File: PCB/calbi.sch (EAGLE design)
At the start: 32 parts, among them U1 LT3086MPT7, U2 33MHZ-OSCILLATOR

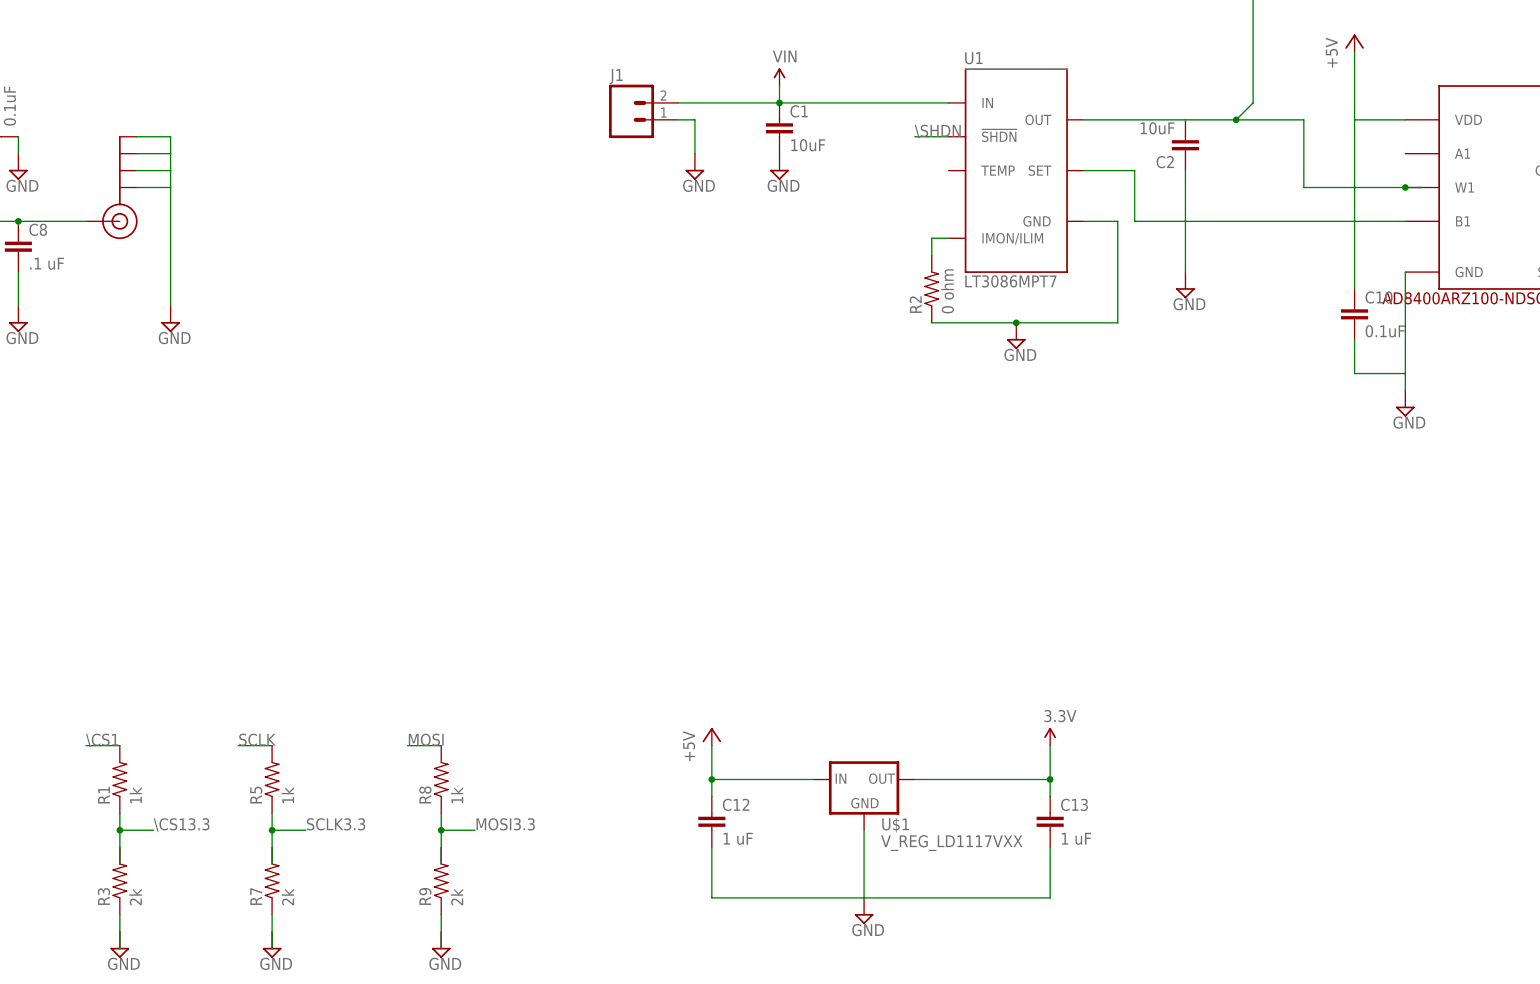
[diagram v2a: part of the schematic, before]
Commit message: Fixed a couple of errors in the schematic. Layed out power. Going to meet on Wednesday at 3:30 to do the RF layout
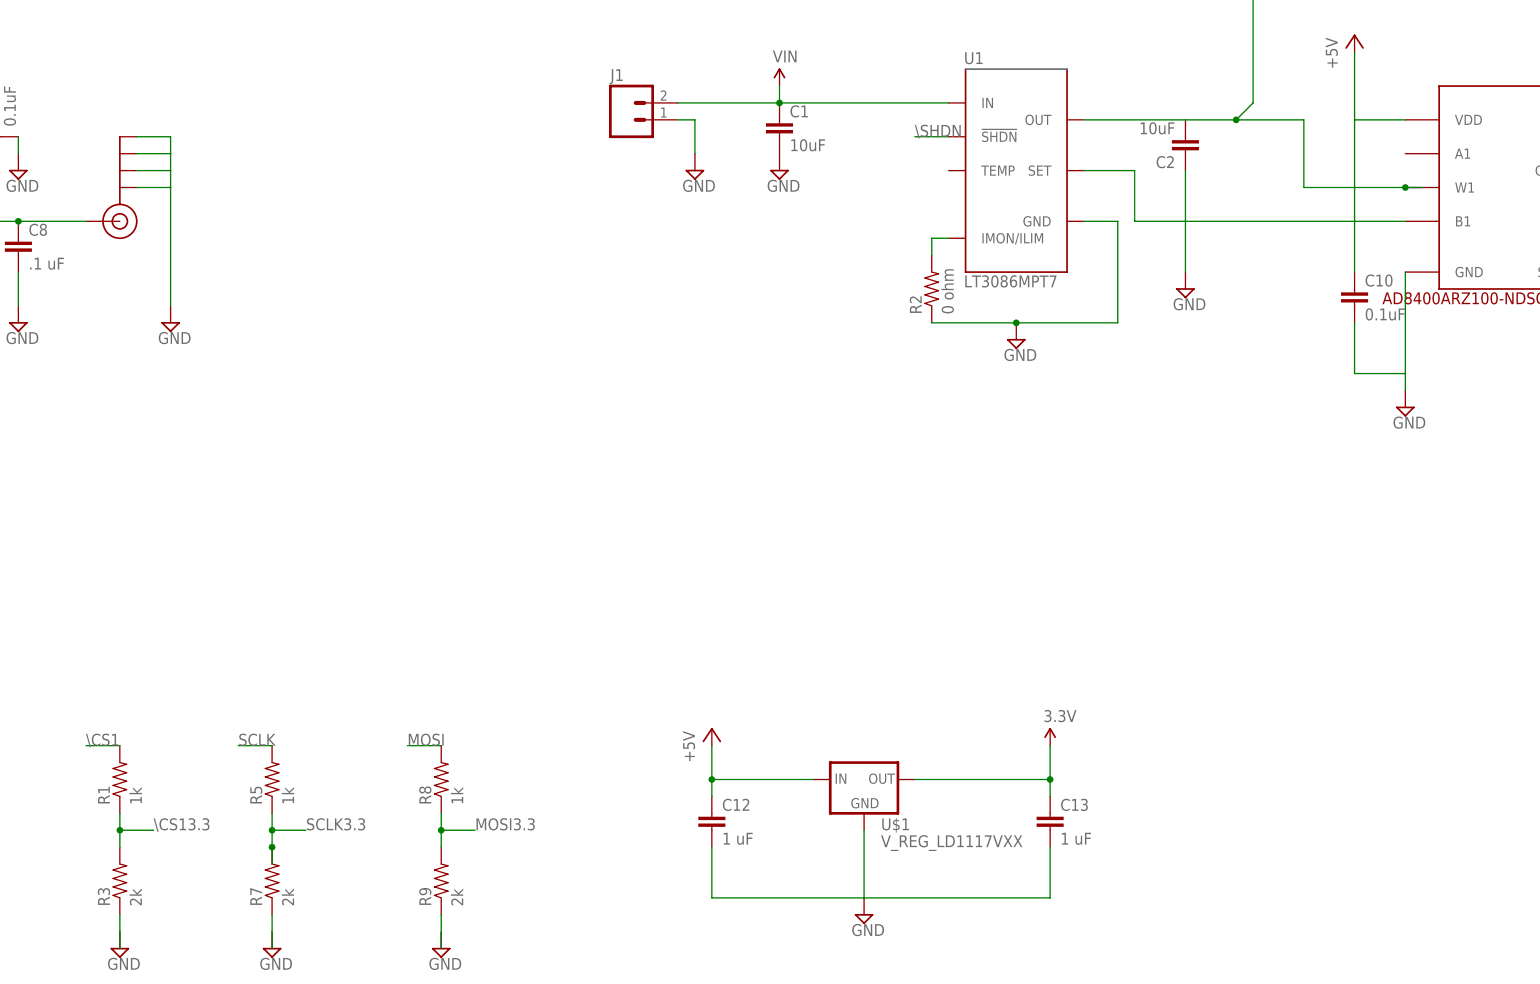
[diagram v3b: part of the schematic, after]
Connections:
- net MOSI3.3: now also R9.2
- net SCLK3.3: now also R7.2
- net \CS13.3: now also R3.2
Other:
- moved on the sheet: C10
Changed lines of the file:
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@@
 <instance part="U$3" gate="G$1" x="149.86" y="198.12" rot="MR0"/>
 <instance part="C2" gate="G$1" x="101.6" y="210.82" rot="R180"/>
-<instance part="C10" gate="G$1" x="127" y="182.88"/>
+<instance part="C10" gate="G$1" x="127" y="185.42"/>
 <instance part="SUPPLY14" gate="GND" x="134.62" y="170.18"/>
 <instance part="SUPPLY16" gate="GND" x="101.6" y="187.96"/>
@@
 <pinref part="C10" gate="G$1" pin="2"/>
 <wire x1="134.62" y1="175.26" x2="134.62" y2="172.72" width="0.1524" layer="91"/>
-<wire x1="127" y1="180.34" x2="127" y2="175.26" width="0.1524" layer="91"/>
+<wire x1="127" y1="182.88" x2="127" y2="175.26" width="0.1524" layer="91"/>
 <wire x1="127" y1="175.26" x2="134.62" y2="175.26" width="0.1524" layer="91"/>
 </segment>
@@
 <pinref part="U$3" gate="G$1" pin="VDD"/>
 <wire x1="134.62" y1="213.36" x2="127" y2="213.36" width="0.1524" layer="91"/>
-<wire x1="127" y1="213.36" x2="127" y2="187.96" width="0.1524" layer="91"/>
+<wire x1="127" y1="213.36" x2="127" y2="190.5" width="0.1524" layer="91"/>
 <pinref part="C10" gate="G$1" pin="1"/>
 <pinref part="P+1" gate="1" pin="+5V"/>
@@
 <pinref part="R5" gate="G$1" pin="1"/>
 <wire x1="-35.56" y1="109.22" x2="-35.56" y2="106.68" width="0.1524" layer="91"/>
-<wire x1="-35.56" y1="106.68" x2="-35.56" y2="101.6" width="0.1524" layer="91"/>
 <wire x1="-35.56" y1="106.68" x2="-30.48" y2="106.68" width="0.1524" layer="91"/>
+<label x="-30.48" y="106.68" size="1.778" layer="95"/>
+<pinref part="R7" gate="G$1" pin="2"/>
+<wire x1="-35.56" y1="104.14" x2="-35.56" y2="101.6" width="0.1524" layer="91"/>
+<wire x1="-35.56" y1="106.68" x2="-35.56" y2="104.14" width="0.1524" layer="91"/>
 <junction x="-35.56" y="106.68"/>
-<label x="-30.48" y="106.68" size="1.778" layer="95"/>
+<junction x="-35.56" y="104.14"/>
 </segment>
 </net>
@@
 <pinref part="R8" gate="G$1" pin="1"/>
 <wire x1="-10.16" y1="109.22" x2="-10.16" y2="106.68" width="0.1524" layer="91"/>
-<wire x1="-10.16" y1="106.68" x2="-10.16" y2="101.6" width="0.1524" layer="91"/>
 <wire x1="-10.16" y1="106.68" x2="-5.08" y2="106.68" width="0.1524" layer="91"/>
+<label x="-5.08" y="106.68" size="1.778" layer="95"/>
+<pinref part="R9" gate="G$1" pin="2"/>
+<wire x1="-10.16" y1="106.68" x2="-10.16" y2="104.14" width="0.1524" layer="91"/>
 <junction x="-10.16" y="106.68"/>
-<label x="-5.08" y="106.68" size="1.778" layer="95"/>
 </segment>
 </net>
@@
 <pinref part="R1" gate="G$1" pin="1"/>
 <wire x1="-58.42" y1="109.22" x2="-58.42" y2="106.68" width="0.1524" layer="91"/>
-<wire x1="-58.42" y1="106.68" x2="-58.42" y2="101.6" width="0.1524" layer="91"/>
 <wire x1="-58.42" y1="106.68" x2="-53.34" y2="106.68" width="0.1524" layer="91"/>
+<label x="-53.34" y="106.68" size="1.778" layer="95"/>
+<pinref part="R3" gate="G$1" pin="2"/>
+<wire x1="-58.42" y1="106.68" x2="-58.42" y2="104.14" width="0.1524" layer="91"/>
 <junction x="-58.42" y="106.68"/>
-<label x="-53.34" y="106.68" size="1.778" layer="95"/>
-</segment>
-</net>
+</segment>
+</net>

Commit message: Commiting changes from Wednesday
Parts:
- C11: value .1 uF -> 0.1uF
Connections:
- net 3.3V: now also C11.1; no longer U2.GND
- net GND: now also C11.2, U2.GND
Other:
- moved on the sheet: C11
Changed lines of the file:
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@@
 <part name="SUPPLY16" library="supply2" deviceset="GND" device=""/>
 <part name="U2" library="SparkFun-FreqCtrl" deviceset="33MHZ-OSCILLATOR" device=""/>
-<part name="C11" library="SparkFun-Capacitors" deviceset="CAP" device="0603-CAP" value=".1 uF"/>
 <part name="SUPPLY17" library="supply2" deviceset="GND" device=""/>
 <part name="SUPPLY18" library="SparkFun-Aesthetics" deviceset="3.3V" device=""/>
@@
 <part name="P+3" library="supply1" deviceset="+5V" device=""/>
 <part name="SUPPLY27" library="SparkFun-Aesthetics" deviceset="3.3V" device=""/>
+<part name="C11" library="SparkFun-Capacitors" deviceset="CAP" device="0603-CAP" value="0.1uF"/>
+<part name="SUPPLY28" library="supply2" deviceset="GND" device=""/>
 </parts>
 <sheets>
@@
 <instance part="SUPPLY16" gate="GND" x="101.6" y="187.96"/>
 <instance part="U2" gate="G$1" x="-152.4" y="165.1"/>
-<instance part="C11" gate="G$1" x="-177.8" y="163.068"/>
-<instance part="SUPPLY17" gate="GND" x="-177.8" y="154.94"/>
+<instance part="SUPPLY17" gate="GND" x="-177.8" y="144.78"/>
 <instance part="SUPPLY18" gate="G$1" x="-177.8" y="172.72"/>
 <instance part="P+1" gate="1" x="127" y="226.06"/>
@@
 <instance part="P+3" gate="1" x="30.48" y="121.92"/>
 <instance part="SUPPLY27" gate="G$1" x="81.28" y="119.38"/>
+<instance part="C11" gate="G$1" x="-177.8" y="157.48"/>
+<instance part="SUPPLY28" gate="GND" x="-139.7" y="154.94"/>
 </instances>
 <busses>
@@
 <wire x1="-177.8" y1="172.72" x2="-177.8" y2="167.64" width="0.1524" layer="91"/>
 <pinref part="U2" gate="G$1" pin="VCC"/>
-<wire x1="-177.8" y1="167.64" x2="-177.8" y2="157.48" width="0.1524" layer="91"/>
-<wire x1="-177.8" y1="157.48" x2="-177.8" y2="154.94" width="0.1524" layer="91"/>
 <wire x1="-165.1" y1="167.64" x2="-177.8" y2="167.64" width="0.1524" layer="91"/>
 <junction x="-177.8" y="167.64"/>
-<pinref part="U2" gate="G$1" pin="GND"/>
-<wire x1="-139.7" y1="162.56" x2="-139.7" y2="157.48" width="0.1524" layer="91"/>
-<wire x1="-139.7" y1="157.48" x2="-177.8" y2="157.48" width="0.1524" layer="91"/>
-<junction x="-177.8" y="157.48"/>
+<pinref part="C11" gate="G$1" pin="1"/>
+<wire x1="-177.8" y1="162.56" x2="-177.8" y2="167.64" width="0.1524" layer="91"/>
 </segment>
 <segment>
@@
 </segment>
 <segment>
-<pinref part="C9" gate="G$1" pin="2"/>
-<pinref part="SUPPLY15" gate="GND" pin="GND"/>
-<wire x1="-96.52" y1="114.3" x2="-96.52" y2="111.76" width="0.1524" layer="91"/>
-</segment>
-<segment>
 <pinref part="SUPPLY20" gate="GND" pin="GND"/>
 <pinref part="_1" gate="G$1" pin="_GND"/>
@@
 <wire x1="81.28" y1="96.52" x2="81.28" y2="104.14" width="0.1524" layer="91"/>
 </segment>
+<segment>
+<pinref part="SUPPLY17" gate="GND" pin="GND"/>
+<wire x1="-177.8" y1="154.94" x2="-177.8" y2="147.32" width="0.1524" layer="91"/>
+<pinref part="C11" gate="G$1" pin="2"/>
+</segment>
+<segment>
+<pinref part="U2" gate="G$1" pin="GND"/>
+<wire x1="-139.7" y1="162.56" x2="-139.7" y2="157.48" width="0.1524" layer="91"/>
+<pinref part="SUPPLY28" gate="GND" pin="GND"/>
+</segment>
+<segment>
+<pinref part="C9" gate="G$1" pin="2"/>
+<pinref part="SUPPLY15" gate="GND" pin="GND"/>
+<wire x1="-96.52" y1="114.3" x2="-96.52" y2="111.76" width="0.1524" layer="91"/>
+</segment>
 </net>

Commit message: FInished up a few things. Set up the cam.
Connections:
- removed net N$12: R7.1
- removed net N$13: R9.1
- removed net N$9: R3.1
- net GND: now also R3.1, R7.1, R9.1
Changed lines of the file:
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@@
 <instance part="R1" gate="G$1" x="-58.42" y="114.3" rot="R90"/>
 <instance part="R3" gate="G$1" x="-58.42" y="99.06" rot="R90"/>
-<instance part="SUPPLY21" gate="GND" x="-58.42" y="88.9"/>
+<instance part="SUPPLY21" gate="GND" x="-58.42" y="83.82"/>
 <instance part="R5" gate="G$1" x="-35.56" y="114.3" rot="R90"/>
 <instance part="R7" gate="G$1" x="-35.56" y="99.06" rot="R90"/>
-<instance part="SUPPLY22" gate="GND" x="-35.56" y="88.9"/>
+<instance part="SUPPLY22" gate="GND" x="-35.56" y="83.82"/>
 <instance part="R8" gate="G$1" x="-10.16" y="114.3" rot="R90"/>
 <instance part="R9" gate="G$1" x="-10.16" y="99.06" rot="R90"/>
-<instance part="SUPPLY23" gate="GND" x="-10.16" y="88.9"/>
+<instance part="SUPPLY23" gate="GND" x="-10.16" y="83.82"/>
 <instance part="SUPPLY24" gate="G$1" x="40.64" y="218.44"/>
 <instance part="J1" gate="G$1" x="17.78" y="213.36"/>
@@
 <wire x1="-96.52" y1="114.3" x2="-96.52" y2="111.76" width="0.1524" layer="91"/>
 </segment>
+<segment>
+<pinref part="R7" gate="G$1" pin="1"/>
+<wire x1="-35.56" y1="93.98" x2="-35.56" y2="86.36" width="0.1524" layer="91"/>
+<pinref part="SUPPLY22" gate="GND" pin="GND"/>
+</segment>
+<segment>
+<pinref part="R9" gate="G$1" pin="1"/>
+<wire x1="-10.16" y1="93.98" x2="-10.16" y2="86.36" width="0.1524" layer="91"/>
+<pinref part="SUPPLY23" gate="GND" pin="GND"/>
+</segment>
+<segment>
+<pinref part="R3" gate="G$1" pin="1"/>
+<wire x1="-58.42" y1="93.98" x2="-58.42" y2="86.36" width="0.1524" layer="91"/>
+<pinref part="SUPPLY21" gate="GND" pin="GND"/>
+</segment>
 </net>
 <net name="N$4" class="0">
@@
 </segment>
 </net>
-<net name="N$9" class="0">
-<segment>
-<pinref part="R3" gate="G$1" pin="1"/>
-<wire x1="-58.42" y1="93.98" x2="-58.42" y2="88.9" width="0.1524" layer="91"/>
-</segment>
-</net>
-<net name="N$12" class="0">
-<segment>
-<pinref part="R7" gate="G$1" pin="1"/>
-<wire x1="-35.56" y1="93.98" x2="-35.56" y2="88.9" width="0.1524" layer="91"/>
-</segment>
-</net>
-<net name="N$13" class="0">
-<segment>
-<pinref part="R9" gate="G$1" pin="1"/>
-<wire x1="-10.16" y1="93.98" x2="-10.16" y2="88.9" width="0.1524" layer="91"/>
-</segment>
-</net>
